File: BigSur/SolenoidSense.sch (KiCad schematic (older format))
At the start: 12 parts, among them U4 ACS70331EOLCTR, U5 ACS70331EOLCTR, U6 ACS70331EOLCTR, U7 ACS70331EOLCTR, U8 ACS70331EOLCTR, U9 ACS70331EOLCTR

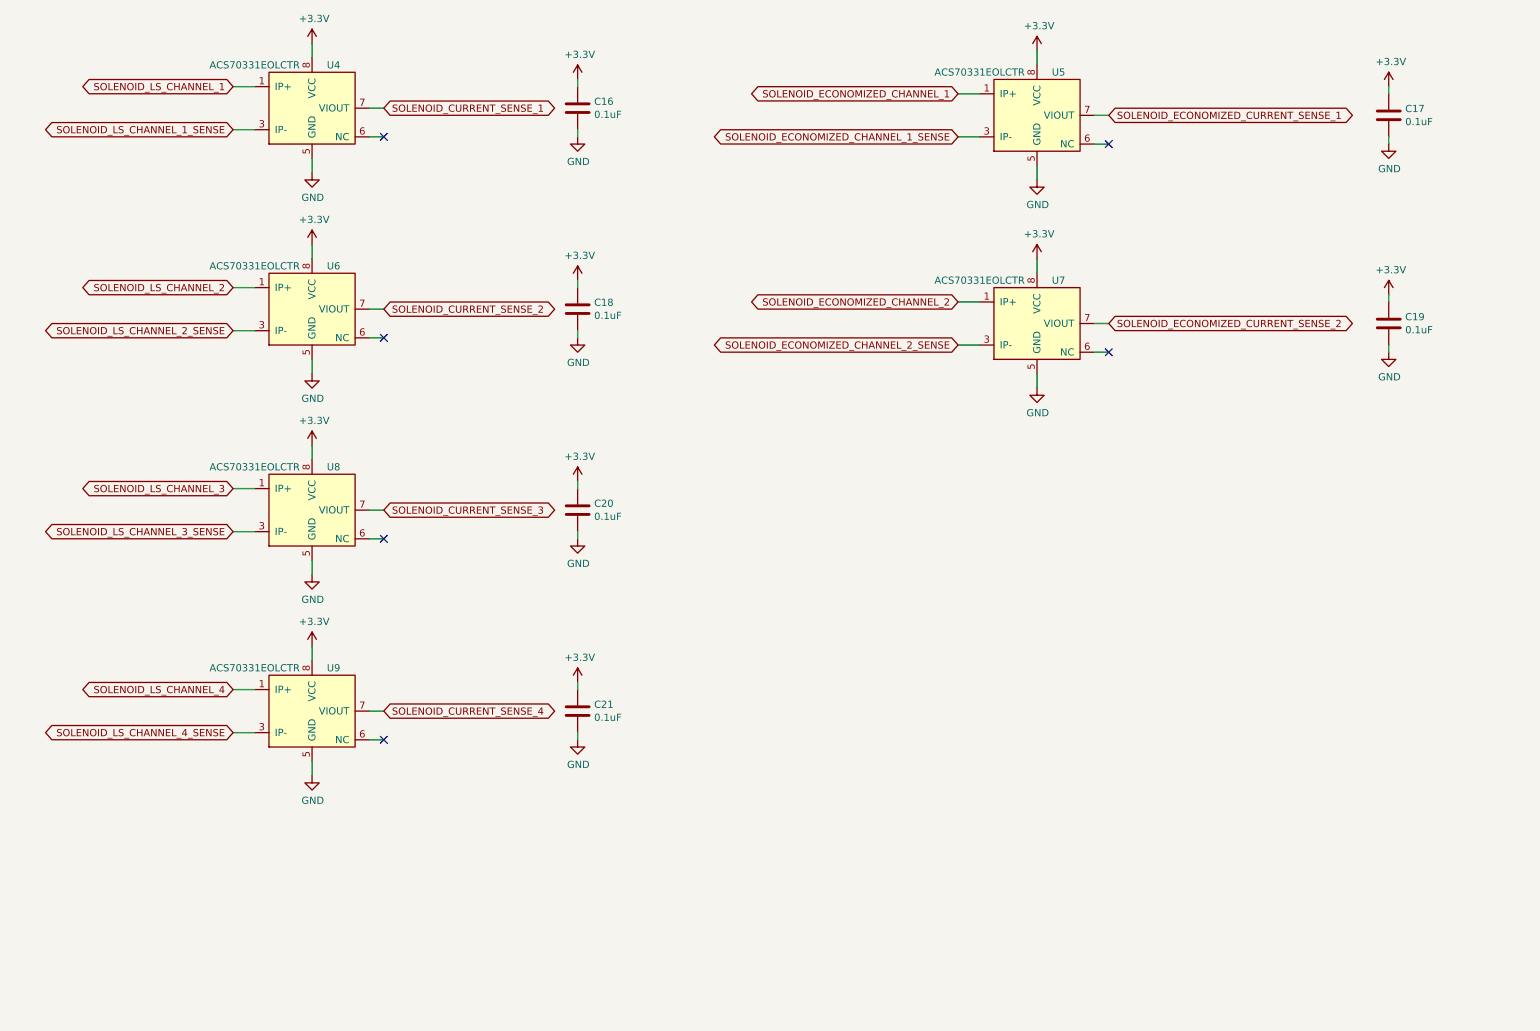
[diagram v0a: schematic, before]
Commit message: Added mounting holes, CAN connector,  indicator LEDs, started general purpose relays
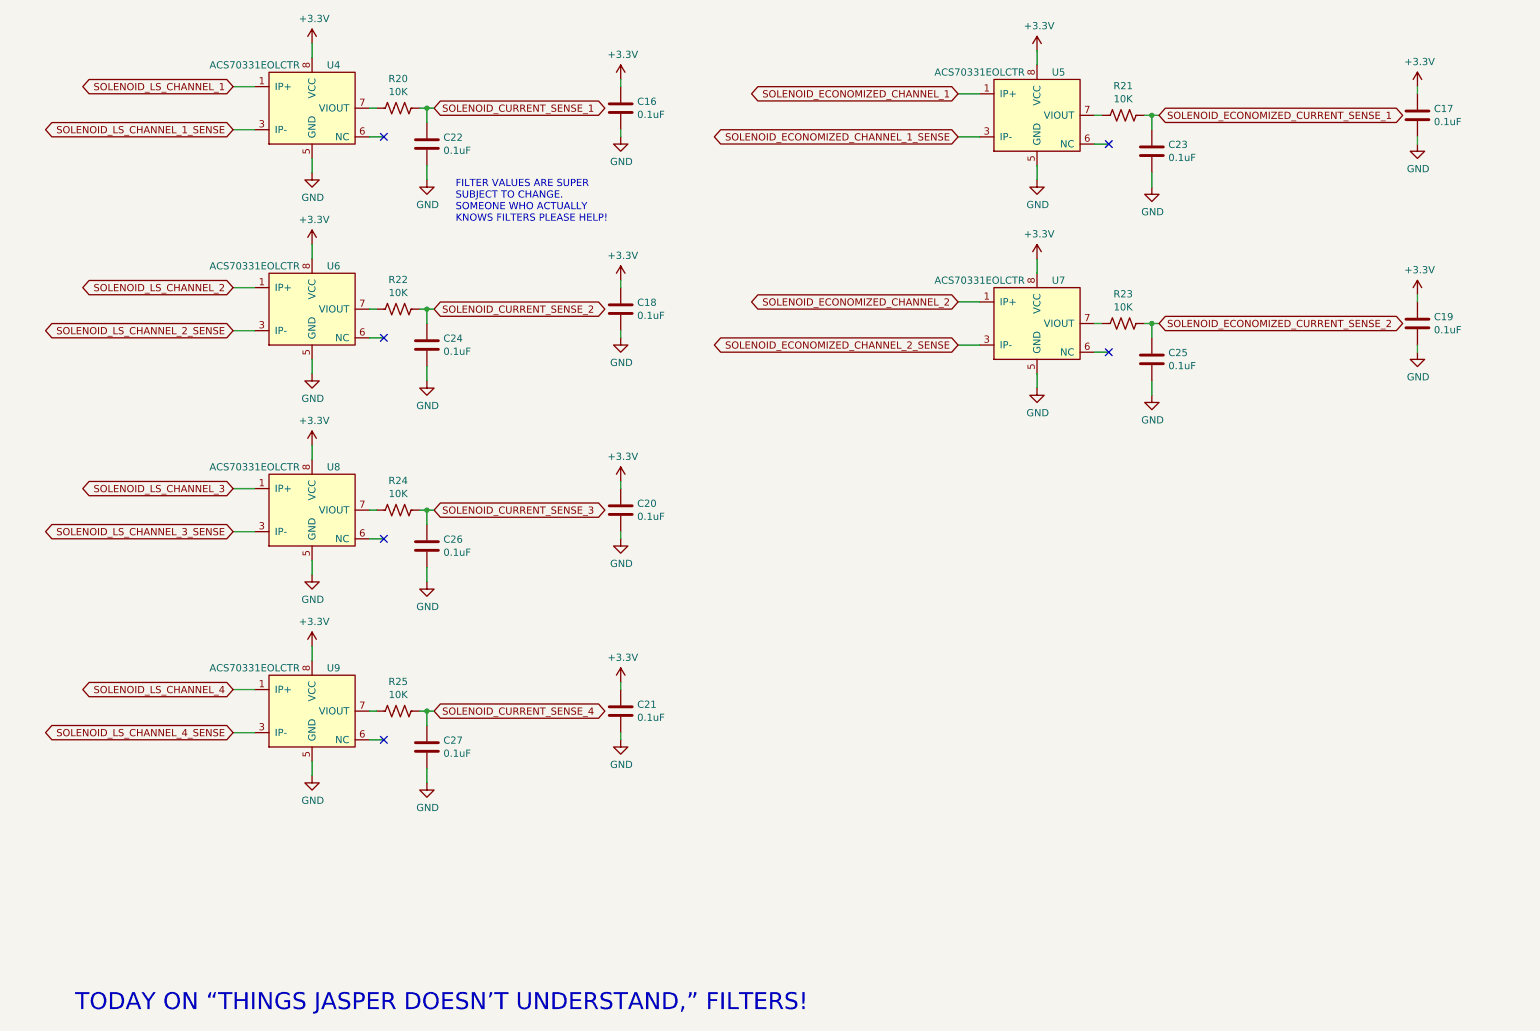
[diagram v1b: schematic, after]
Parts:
- added C22, C23, C24, C25, C26, C27: 0.1uF, Capacitor_SMD:C_0603_1608Metric_Pad1.05x0.95mm_HandSolder, symbol Device:C
- added R20, R21, R22, R23, R24, R25: 10K, symbol Device:R_US
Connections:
- net GND: now also C22.2, C23.2, C24.2, C25.2, C26.2, C27.2
- net SOLENOID_CURRENT_SENSE_1: now also C22.1, R20.1; no longer U4.7 (VIOUT)
- net SOLENOID_CURRENT_SENSE_2: now also C24.1, R22.1; no longer U6.7 (VIOUT)
- net SOLENOID_CURRENT_SENSE_3: now also C26.1, R24.1; no longer U8.7 (VIOUT)
- net SOLENOID_CURRENT_SENSE_4: now also C27.1, R25.1; no longer U9.7 (VIOUT)
- net SOLENOID_ECONOMIZED_CURRENT_SENSE_1: now also C23.1, R21.1; no longer U5.7 (VIOUT)
- net SOLENOID_ECONOMIZED_CURRENT_SENSE_2: now also C25.1, R23.1; no longer U7.7 (VIOUT)
- new net: R20.2, U4.7 (VIOUT)
- new net: R22.2, U6.7 (VIOUT)
- new net: R24.2, U8.7 (VIOUT)
- new net: R25.2, U9.7 (VIOUT)
- new net: R21.2, U5.7 (VIOUT)
- new net: R23.2, U7.7 (VIOUT)
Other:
- note added: "FILTER VALUES ARE SUPER\nSUBJECT TO CHANGE.\nSOMEONE WHO ACTUALLY\nKNOWS FILTERS PLEASE HELP!"
- note added: "TODAY ON “THINGS JASPER DOESN’T UNDERSTAND,” FILTERS!"
- moved on the sheet: C16, C17, C18, C19, C20, C21

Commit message: Updated test points
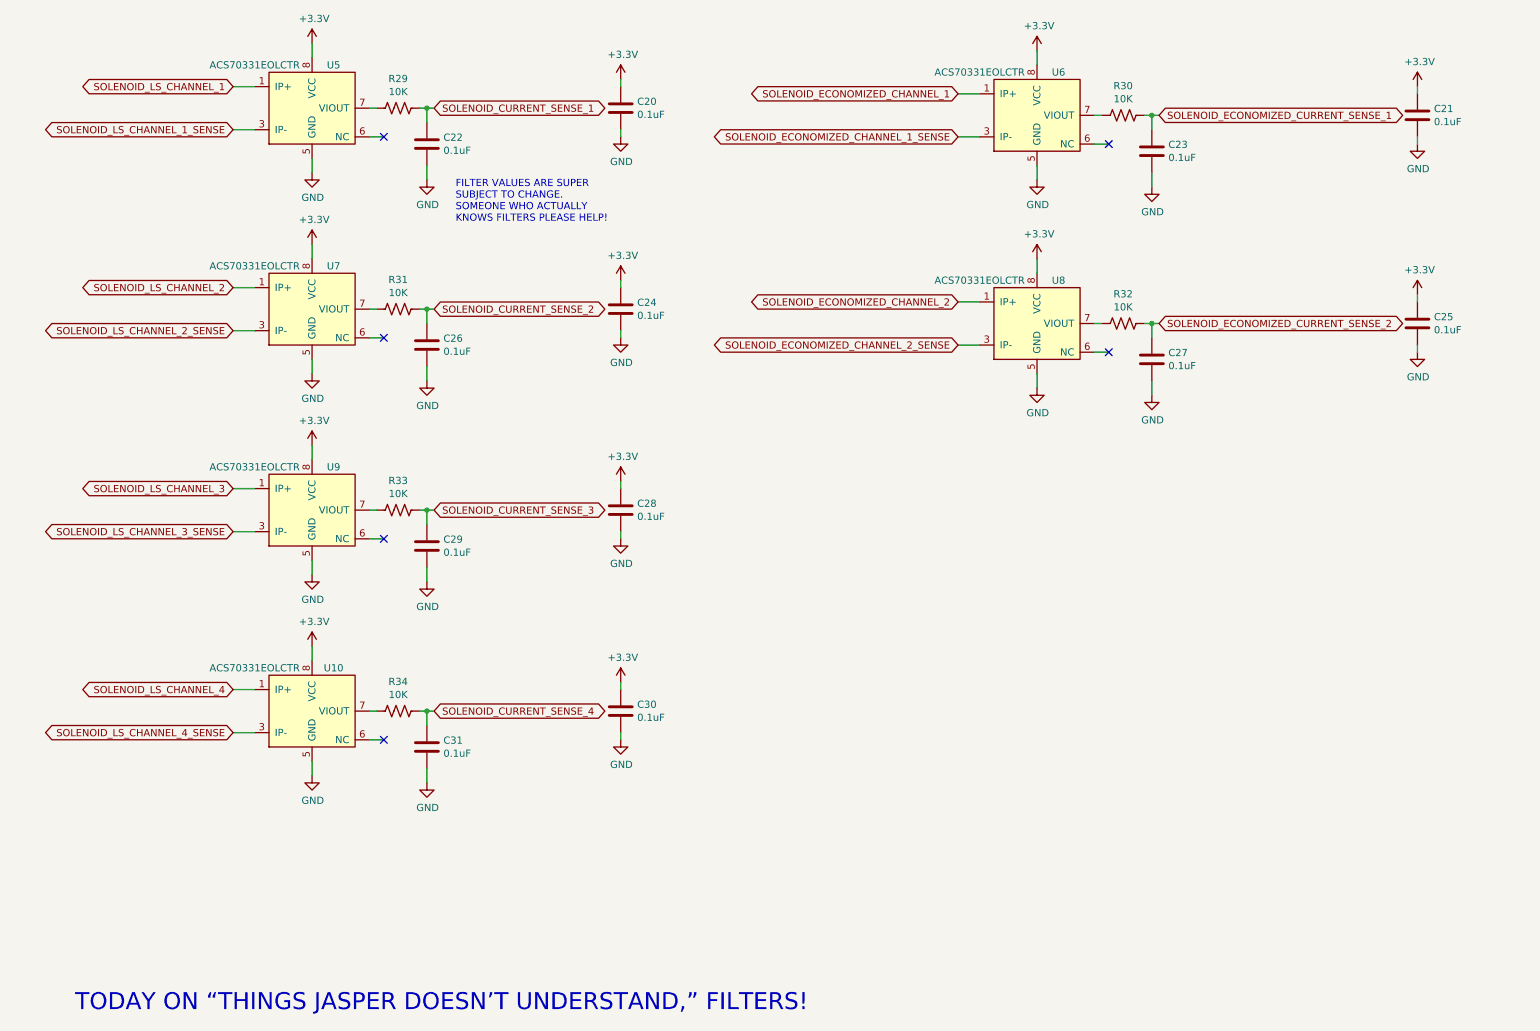
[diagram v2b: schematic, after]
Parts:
- removed R21, R22, R23, R24, R25: 10K, symbol Device:R_US
- added R30, R31, R32, R33, R34: 10K, Resistor_SMD:R_0603_1608Metric_Pad1.05x0.95mm_HandSolder, symbol Device:R_US
- R29: renamed from R20; footprint (none) -> Resistor_SMD:R_0603_1608Metric_Pad1.05x0.95mm_HandSolder; Digikey (none) -> https://www.digikey.ca/product-detail/en/stackpole-electron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; Part Number (none) -> RNCP0603FTD10K0
- renumbered C16 to C20, C17 to C21, C18 to C24, C19 to C25, C24 to C26, C25 to C27, C20 to C28, C26 to C29, C21 to C30, C27 to C31, U9 to U10, U4 to U5, U5 to U6, U6 to U7, U7 to U8, U8 to U9
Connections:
- net SOLENOID_CURRENT_SENSE_2: now also R31.1
- net SOLENOID_CURRENT_SENSE_3: now also R33.1
- net SOLENOID_CURRENT_SENSE_4: now also R34.1
- net SOLENOID_ECONOMIZED_CURRENT_SENSE_1: now also R30.1
- net SOLENOID_ECONOMIZED_CURRENT_SENSE_2: now also R32.1
- net at U7.7 (VIOUT): now also R31.2
- net at U9.7 (VIOUT): now also R33.2
- net at U10.7 (VIOUT): now also R34.2
- net at U6.7 (VIOUT): now also R30.2
- net at U8.7 (VIOUT): now also R32.2

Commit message: Added braking detection, relay flyback, changed current sensors.
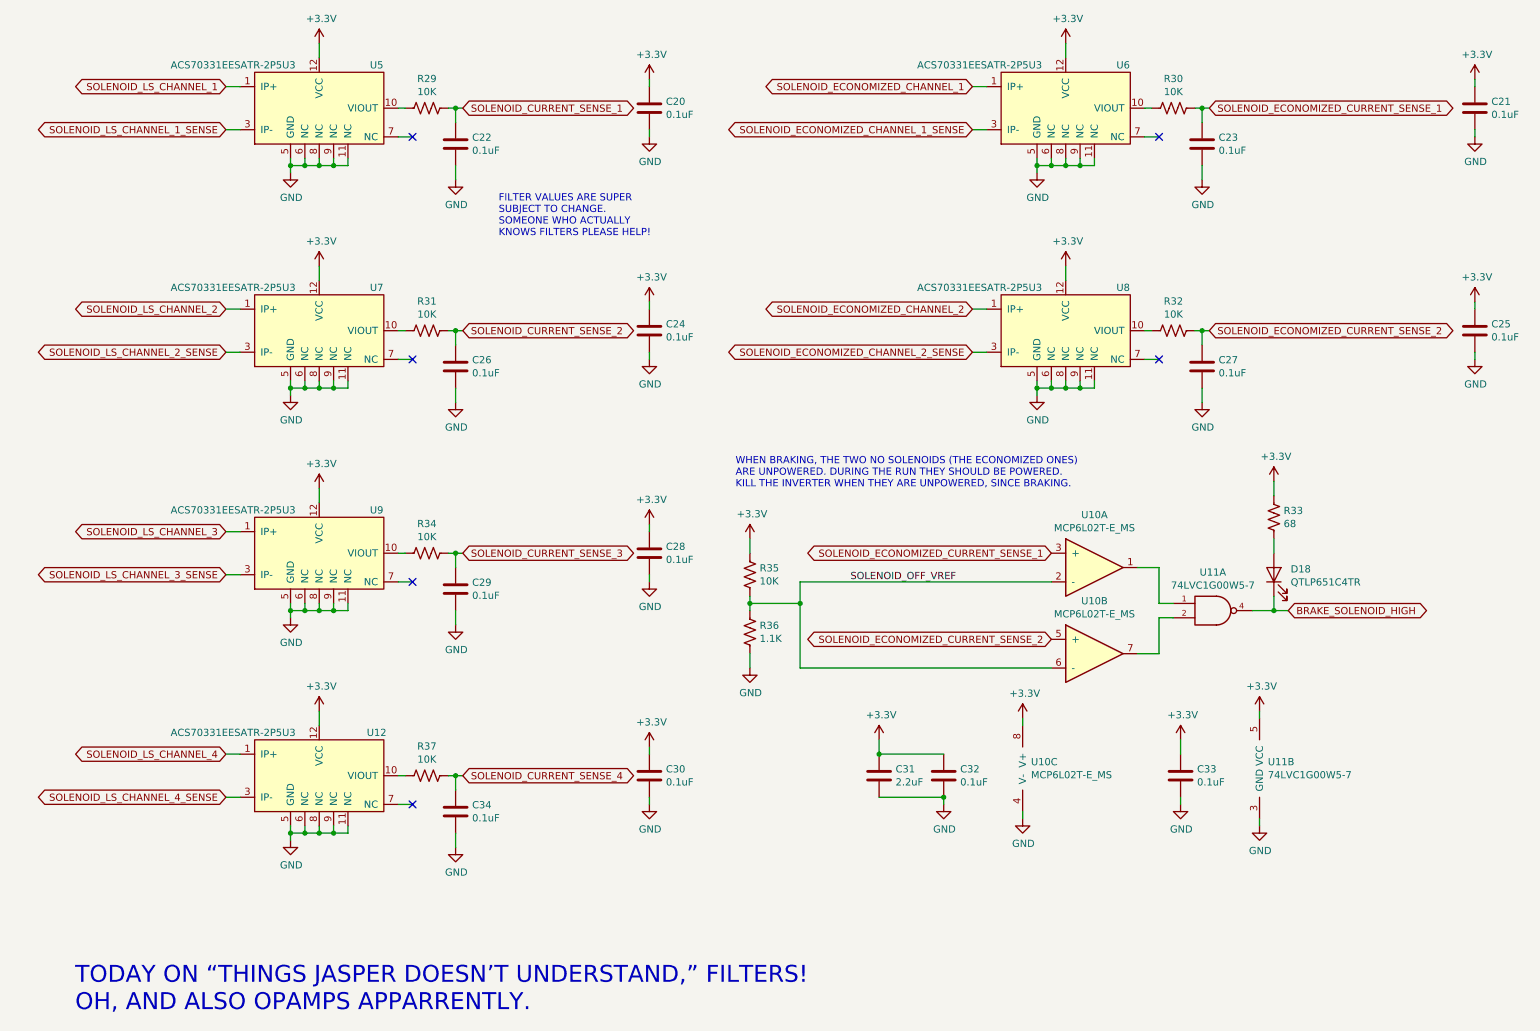
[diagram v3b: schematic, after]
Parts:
- removed U10, U5, U6, U7, U8, U9: ACS70331EOLCTR, BigSur:Allegro_SOIC_6.2x5.0mm_P1.27mm, symbol BigSurLib:ACS70331EOLCTR
- added C32, C33, C34: 0.1uF, Capacitor_SMD:C_0603_1608Metric_Pad1.05x0.95mm_HandSolder, symbol Device:C
- added D18: QTLP651C4TR, LED_SMD:LED_1206_3216Metric_Pad1.42x1.75mm_HandSolder, symbol Device:LED
- added R35, R37: 10K, Resistor_SMD:R_0603_1608Metric_Pad1.05x0.95mm_HandSolder, symbol Device:R_US
- added R36: 1.1K, Resistor_SMD:R_0603_1608Metric_Pad1.05x0.95mm_HandSolder, symbol Device:R_US
- added U10: MCP6L02T-E_MS, Package_SO:MSOP-8_3x3mm_P0.65mm, symbol BigSurLib:MCP6L02T-E_MS
- added U11: 74LVC1G00W5-7, Package_TO_SOT_SMD:SOT-23-5, symbol BigSurLib:74LVC1G00W5-7
- added U12, U5, U6, U7, U8, U9: ACS70331EESATR-2P5U3, BigSur:Allegro_QFN_ACS70331EESATR, symbol BigSurLib:ACS70331EESATR-2P5U3
- C31: value 0.1uF -> 2.2uF
- R33: value 10K -> 68; Digikey https://www.digikey.ca/product-detail/en/stackpole-electron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 -> https://www.digikey.ca/product-detail/en/rohm-semiconductor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; Part Number RNCP0603FTD10K0 -> ESR03EZPJ680
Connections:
- net +3V3: now also C31.1, R33.1, C32.1, C33.1, R35.1, U10.8 (V+), U11.5 (VCC), U12.12 (VCC), U5.12 (VCC), U6.12 (VCC), U7.12 (VCC), U8.12 (VCC), U9.12 (VCC)
- net GND: now also C32.2, C33.2, C34.2, R36.2, U10.4 (V-), U11.3 (GND), U12.11 (NC), U12.5 (GND), U12.6 (NC), U12.8 (NC), U12.9 (NC), U5.11 (NC), U5.5 (GND), U5.6 (NC), U5.8 (NC), U5.9 (NC), U6.11 (NC), U6.5 (GND), U6.6 (NC), U6.8 (NC), U6.9 (NC), U7.11 (NC), U7.5 (GND), U7.6 (NC), U7.8 (NC), U7.9 (NC), U8.11 (NC), U8.5 (GND), U8.6 (NC), U8.8 (NC), U8.9 (NC), U9.11 (NC), U9.5 (GND), U9.6 (NC), U9.8 (NC), U9.9 (NC)
- net SOLENOID_CURRENT_SENSE_3: now also R34.1; no longer R33.1
- net SOLENOID_CURRENT_SENSE_4: now also C34.1, R37.1; no longer C31.1, R34.1
- net SOLENOID_ECONOMIZED_CHANNEL_1: now also U6.1 (IP+)
- net SOLENOID_ECONOMIZED_CHANNEL_1_SENSE: now also U6.3 (IP-)
- net SOLENOID_ECONOMIZED_CHANNEL_2: now also U8.1 (IP+)
- net SOLENOID_ECONOMIZED_CHANNEL_2_SENSE: now also U8.3 (IP-)
- net SOLENOID_ECONOMIZED_CURRENT_SENSE_1: now also U10.3 (+)
- net SOLENOID_ECONOMIZED_CURRENT_SENSE_2: now also U10.5 (+)
- net SOLENOID_LS_CHANNEL_1: now also U5.1 (IP+)
- net SOLENOID_LS_CHANNEL_1_SENSE: now also U5.3 (IP-)
- net SOLENOID_LS_CHANNEL_2: now also U7.1 (IP+)
- net SOLENOID_LS_CHANNEL_2_SENSE: now also U7.3 (IP-)
- net SOLENOID_LS_CHANNEL_3: now also U9.1 (IP+)
- net SOLENOID_LS_CHANNEL_3_SENSE: now also U9.3 (IP-)
- net SOLENOID_LS_CHANNEL_4: now also U12.1 (IP+)
- net SOLENOID_LS_CHANNEL_4_SENSE: now also U12.3 (IP-)
- net at R29.2: now also U5.10 (VIOUT)
- net at R31.2: now also U7.10 (VIOUT)
- net at R33.2: now also D18.2 (A)
- net at R32.2: now also U8.10 (VIOUT)
- net at R30.2: now also U6.10 (VIOUT)
- net at R34.2: now also U9.10 (VIOUT)
- new net: U10.1, U11.1
- new net: U10.7, U11.2
- new net: R37.2, U12.10 (VIOUT)
- new net BRAKE_SOLENOID_HIGH: D18.1 (K), U11.4
- new net SOLENOID_OFF_VREF: R35.2, R36.1, U10.2 (-), U10.6 (-)
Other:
- note added: "TODAY ON “THINGS JASPER DOESN’T UNDERSTAND,” FILTERS!\nOH, AND ALSO OPAMPS APPARRENTLY."
- note added: "WHEN BRAKING, THE TWO NO SOLENOIDS (THE ECONOMIZED ONES)\nARE UNPOWERED. DURING THE RUN THEY SHOULD BE POWERED.\nKILL THE INVERTER WHEN THEY ARE UNPOWERED, SINCE BRAKING."
- note removed: "TODAY ON “THINGS JASPER DOESN’T UNDERSTAND,” FILTERS!"
- moved on the sheet: C20, C22, R29

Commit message: Added to self deprecation.
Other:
- note added: "FILTER VALUES ARE SUPER SUBJECT TO CHANGE.\nSOMEONE WHO ACTUALLY KNOWS FILTERS\nPLEASE LET ME KNOW IF THESE VALUES ARE WEIRD."
- note added: "TODAY ON “THINGS JASPER DOESN’T UNDERSTAND,” FILTERS!\nOH, AND ALSO OPAMPS APPARRENTLY. GOOD TIMES."
- note removed: "FILTER VALUES ARE SUPER\nSUBJECT TO CHANGE.\nSOMEONE WHO ACTUALLY\nKNOWS FILTERS PLEASE HELP!"
- note removed: "TODAY ON “THINGS JASPER DOESN’T UNDERSTAND,” FILTERS!\nOH, AND ALSO OPAMPS APPARRENTLY."
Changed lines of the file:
@@
 	3450 1750 3450 1650
 Text Notes 800  7550 0    118  ~ 0
-TODAY ON “THINGS JASPER DOESN’T UNDERSTAND,” FILTERS!\nOH, AND ALSO OPAMPS APPARRENTLY.
+TODAY ON “THINGS JASPER DOESN’T UNDERSTAND,” FILTERS!\nOH, AND ALSO OPAMPS APPARRENTLY. GOOD TIMES.
 Text Notes 3750 2150 0    50   ~ 0
-FILTER VALUES ARE SUPER\nSUBJECT TO CHANGE.\nSOMEONE WHO ACTUALLY\nKNOWS FILTERS PLEASE HELP!
+FILTER VALUES ARE SUPER SUBJECT TO CHANGE.\nSOMEONE WHO ACTUALLY KNOWS FILTERS\nPLEASE LET ME KNOW IF THESE VALUES ARE WEIRD.
 Text Notes 5400 3900 0    50   ~ 0
 WHEN BRAKING, THE TWO NO SOLENOIDS (THE ECONOMIZED ONES)\nARE UNPOWERED. DURING THE RUN THEY SHOULD BE POWERED.\nKILL THE INVERTER WHEN THEY ARE UNPOWERED, SINCE BRAKING.
